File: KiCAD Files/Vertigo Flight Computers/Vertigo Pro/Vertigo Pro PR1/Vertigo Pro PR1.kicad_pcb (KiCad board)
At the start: 4 copper layers, 133 parts, among them IC1 ICM-20602, IC2 DPS310XTSA1, J1 ST-LINK Conn, J2 USB_C_2.0, J3 FFC2A32-24-T, J4 Screw_Terminal, J5 Screw_Terminal, J6 Screw_Terminal, J7 Screw_Terminal, Q1 IRFL024ZTRPBF, Q2 MMBT3904-TP, Q3 MMBT3904-TP, Q4 IRFL024ZTRPBF, Q5 SI7149ADP-T1-GE3, Q6 MMBT3904-TP, Q7 MMBT3904-TP, Q8 IRFL024ZTRPBF, Q9 IRFL024ZTRPBF, SW1 SW_SPDT, U1 STM32F103C8Tx, U10 TPS79133DBVR, U12 TLV709, U13 TLV75528PDBV, U2 AP63203WU, U3 ESP32-S3-WROOM-1, U4 TLV75515PDBV, U8 NEO-6M-GPS, U9 24AA32A-I_MS, Y1 16MHz

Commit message: prepcb
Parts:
- Q5, U12, U2, U8, U9: moved to B.Cu
- moved J1 109.9 mm to (108.0, 129.7)
- moved U1 72.8 mm to (108.8, 110.5), turned to 45 degrees
- moved J4 71.8 mm to (124.8, 107.5), turned to 90 degrees
- moved J5 71.5 mm to (124.9, 116.2), turned to 90 degrees
- moved J6 69.2 mm to (91.9, 104.0), turned to -90 degrees
- moved D5 69.1 mm to (92.8, 127.5), turned to 180 degrees
- moved J7 69.0 mm to (91.9, 112.8), turned to -90 degrees
- moved U10 62.3 mm to (147.2, 132.5)
- moved FL1 61.9 mm to (97.8, 126.8)
- moved D9 61.0 mm to (93.9, 85.2)
- moved Q6 60.3 mm to (205.4, 92.1)
- moved R17 60.3 mm to (153.4, 103.4)
- moved R25 60.3 mm to (153.4, 123.5)
- moved JP1 60.3 mm to (217.4, 68.8)
- moved JP2 60.3 mm to (217.4, 72.4)
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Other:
- board outline added: 40.8 x 62 mm

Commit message: fix
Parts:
- moved U2 25.6 mm to (137.1, 113.3)
- moved L1 25.3 mm to (142.2, 94.8)
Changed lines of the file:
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@@
 	(footprint "Vertigo Pro KiCad Libraries:CDMC6D28NP-4R7MC"
 		(layer "F.Cu")
-		(at 167.5 93)
+		(at 142.25 94.75)
 		(property "Reference" "L1"
 			(at 0.25 -4 0)
@@
 			(polygon
 				(pts
-					(xy 163.75 91.25) (xy 165.25 91.25) (xy 165.25 94.75) (xy 163.75 94.75)
+					(xy 138.5 93) (xy 140 93) (xy 140 96.5) (xy 138.5 96.5)
 				)
 			)
@@
 	(footprint "Package_TO_SOT_SMD:TSOT-23-6"
 		(layer "B.Cu")
-		(at 153 93.25 180)
+		(at 137.1375 113.3 180)
 		(descr "TSOT, 6 Pin (https://www.jedec.org/sites/default/files/docs/MO-193D.pdf variant AA), generated with kicad-footprint-generator ipc_gullwing_generator.py")
 		(tags "TSOT TO_SOT_SMD")

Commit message: fix
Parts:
- IC1: moved to B.Cu
- moved IC1 29.5 mm to (108.0, 120.5), turned to 180 degrees
- moved IC2 18.1 mm to (93.3, 113.3), turned to 180 degrees
- moved J5 9.25 mm to (124.8, 107.0)
- moved J4 9.25 mm to (124.8, 98.2)
- moved J6 9.01 mm to (92.2, 95.0)
- moved J7 9.01 mm to (92.2, 103.8)
- moved U1 1.59 mm to (108.2, 109.0)
- moved U8 1.58 mm to (108.2, 109.0)
- moved U12 0.75 mm to (113.3, 121.0)
- moved Q5 0.66 mm to (118.5, 122.4)
- moved D9 0.56 mm to (93.3, 85.2)
- moved U3 0.52 mm to (108.2, 88.2)
- moved D8 0.25 mm to (123.5, 85.4)

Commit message: redo
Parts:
- IC1, Q5, U12, U2, U8, U9: moved to F.Cu
- moved J1 166.1 mm to (259.5, 61.7)
- moved D5 160.9 mm to (253.7, 130.6), turned to 0 degrees
- moved D9 159.9 mm to (250.9, 112.2)
- moved U9 153.4 mm to (250.8, 117.8), turned to 0 degrees
- moved IC2 153.3 mm to (245.3, 133.1), turned to 0 degrees
- moved FL1 152.5 mm to (250.3, 128.2)
- moved U1 149.8 mm to (256.2, 85.7), turned to 0 degrees
- moved J6 145.8 mm to (237.5, 82.5), turned to 0 degrees
- moved J7 145.8 mm to (237.5, 91.6), turned to 0 degrees
- moved J2 141.5 mm to (237.2, 132.2)
- moved IC1 137.9 mm to (245.6, 128.7), turned to 0 degrees
- moved J3 133.0 mm to (241.7, 123.5)
- moved D8 129.0 mm to (250.9, 105.5)
- moved Y1 123.5 mm to (225.1, 134.2), turned to 0 degrees
- moved U2 120.8 mm to (257.7, 104.6), turned to 0 degrees
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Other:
- board outline removed

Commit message: Sch fix, prepcb
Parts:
- removed D6: LED, Resistor_SMD:R_0603_1608Metric
- removed J1: ST-LINK Conn, Connector_PinSocket_1.27mm:PinSocket_1x04_P1.27mm_Vertical
- removed J3: FFC2A32-24-T, Vertigo Pro KiCad Libraries:GCT_FFC2A32-24-T
- added CAM: FFC2A32-24-T, Vertigo Pro KiCad Libraries:GCT_FFC2A32-24-T, F.Cu at (148.5, 101.6)
- added GPS LED: LED, Resistor_SMD:R_0603_1608Metric, B.Cu at (138.2, 102.5)
- added SWD: ST-LINK Conn, Connector_PinSocket_1.27mm:PinSocket_1x04_P1.27mm_Vertical, F.Cu at (118.0, 127.0)
- C23, C24, C43, C44, C45, C46, C51, C52, JP1, JP2, Q1, Q2, Q3, Q4, Q6, Q7, Q8, Q9, U10, U13, U4, U8, U9: moved to B.Cu
- R1, R10, R12, R15, R16, R17, R19, R2, R20, R26, R27, R28, R29, R3, R30, R31, R34, R4, R44, R46, R47, R48, R49, R5, R7, R8, R9: footprint Resistor_SMD:R_0603_1608Metric -> Resistor_SMD:R_0805_2012Metric_Pad1.20x1.40mm_HandSolder
- R11, R13, R14, R18, R21, R22, R23, R24, R25, R43, R50, R51, R52, R53, R6: footprint Resistor_SMD:R_0603_1608Metric -> Resistor_SMD:R_0805_2012Metric_Pad1.20x1.40mm_HandSolder; moved to B.Cu
- moved C45 139.7 mm to (129.6, 125.5)
- moved C46 139.5 mm to (129.6, 127.5)
- moved Q3 122.6 mm to (129.0, 119.5), turned to 180 degrees
- moved D9 121.1 mm to (132.6, 86.1), turned to 135 degrees
- moved D3 120.0 mm to (139.8, 139.8), turned to 180 degrees
- moved Q2 118.1 mm to (129.2, 80.3), turned to 180 degrees
- moved D5 117.1 mm to (137.0, 139.5), turned to 90 degrees
- moved JP1 116.3 mm to (143.5, 79.2), turned to 180 degrees
- moved C27 116.1 mm to (157.5, 145.6), turned to -90 degrees
- moved FL1 116.0 mm to (134.8, 139.0), turned to 90 degrees
- moved C23 113.4 mm to (144.0, 107.2)
- moved U1 111.8 mm to (148.5, 115.5), turned to 45 degrees
- moved C51 111.3 mm to (148.0, 99.2), turned to 180 degrees
- moved J4 111.2 mm to (130.3, 94.0), turned to -90 degrees
- moved J5 111.1 mm to (130.3, 102.8), turned to -90 degrees
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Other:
- board outline added: 45.2 x 81.8 mm
- board text added: "Vertigo Pro Dev Board DV1"

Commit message: pcb
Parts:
- SW1: moved to B.Cu
- moved R1 27.5 mm to (155.2, 135.8), turned to -135 degrees
- moved SW1 26.9 mm to (157.8, 131.0), turned to 90 degrees
- moved U1 16.4 mm to (148.5, 131.9), turned to -135 degrees
- moved Y1 13.5 mm to (154.4, 126.8)
- moved IC1 12.0 mm to (148.5, 122.5)
- moved Baro 9.77 mm to (148.5, 117.8)
- renumbered IC2 to Baro
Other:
- board text added: "Vertigo Pro Prototype Dev Board DR1"
- board text removed: "Vertigo Pro Dev Board DV1"

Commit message: pcb
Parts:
- C40, C47, C48, U12: moved to B.Cu
- moved R64 117.3 mm to (132.5, 80.2), turned to 180 degrees
- moved U12 95.3 mm to (148.2, 89.8), turned to -90 degrees
- moved C50 85.5 mm to (136.5, 89.2), turned to 90 degrees
- moved R63 84.9 mm to (164.8, 80.0)
- moved C47 76.9 mm to (144.6, 88.5)
- moved C48 76.8 mm to (144.6, 91.0)
- moved C14 75.5 mm to (186.9, 135.2)
- moved C12 75.5 mm to (186.9, 130.2)
- moved C15 75.5 mm to (186.9, 137.8)
- moved C13 75.5 mm to (186.9, 132.7)
- moved C40 74.5 mm to (147.5, 125.8), turned to 90 degrees
- moved U2 62.7 mm to (179.5, 135.7)
- moved C49 61.7 mm to (160.2, 89.2), turned to -90 degrees
- moved SWD 14.1 mm to (115.7, 113.2)
- moved AE1 5.15 mm to (208.3, 75.5)
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
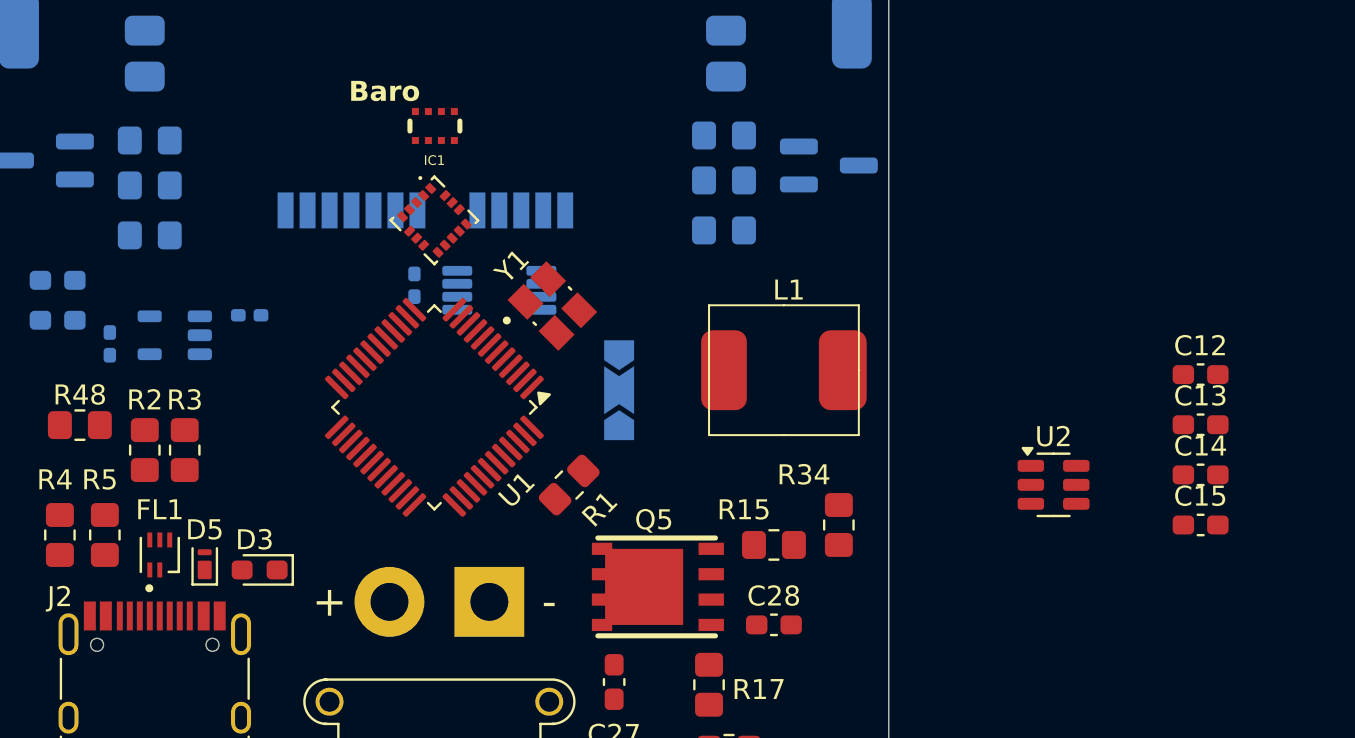
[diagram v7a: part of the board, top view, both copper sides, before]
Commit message: Switching voltage regulator layout
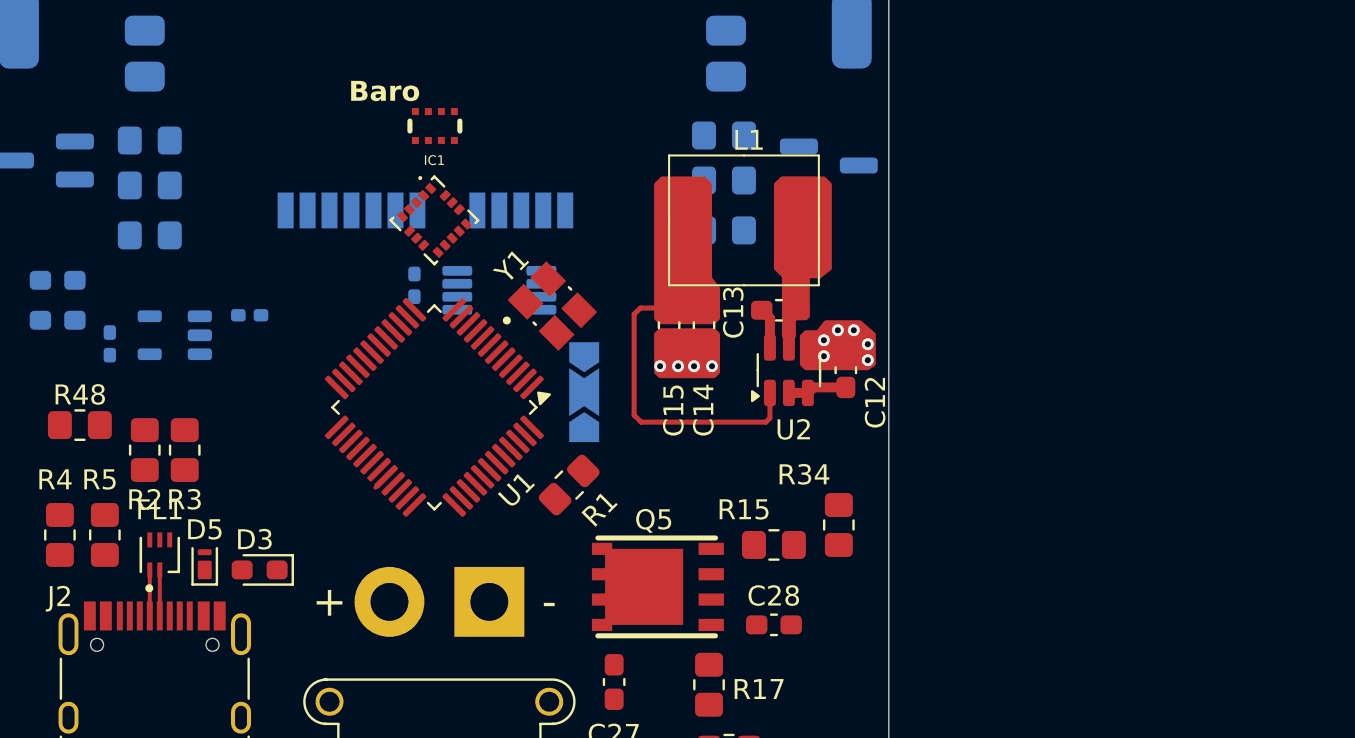
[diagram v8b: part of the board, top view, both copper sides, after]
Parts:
- moved C15 28.4 mm to (160.2, 127.8), turned to -90 degrees
- moved C14 26.0 mm to (162.0, 127.8), turned to -90 degrees
- moved C13 21.9 mm to (165.8, 127.0)
- moved C12 17.8 mm to (169.1, 130.0), turned to 90 degrees
- moved U2 14.4 mm to (166.2, 130.0), turned to 90 degrees
- moved L1 7.76 mm to (164.0, 122.5)
- moved SW1 1.75 mm to (156.0, 131.1)
- turned R2 to 90 degrees
- turned R3 to -90 degrees
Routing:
- net +3.3V: track 0.00 -> 15.2 mm
- net VCC: track 0.00 -> 2.86 mm
- net Net-(FL1-I/O+_IN): track 0.00 -> 2.31 mm
- net Net-(FL1-I/O-_IN): track 0.00 -> 2.31 mm
- net Net-(U2-BST): track 0.00 -> 2.03 mm
- net /USB_D-: track 0.00 -> 0.77 mm
- net AGND: vias 0 -> 10
